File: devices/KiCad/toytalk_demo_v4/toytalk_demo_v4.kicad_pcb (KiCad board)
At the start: 2 copper layers, 55 x 55 mm, 44 parts, among them J1 TYPE-C-31-M-12, J2 Conn_01x02, U1 ESP32-S3-WROOM-1-N8R8, U2 MAX98357AEWL_T, U3 BQ24074RGTR, U4 AP2112K-3.3TRG1, U5 TPS61022RWUR

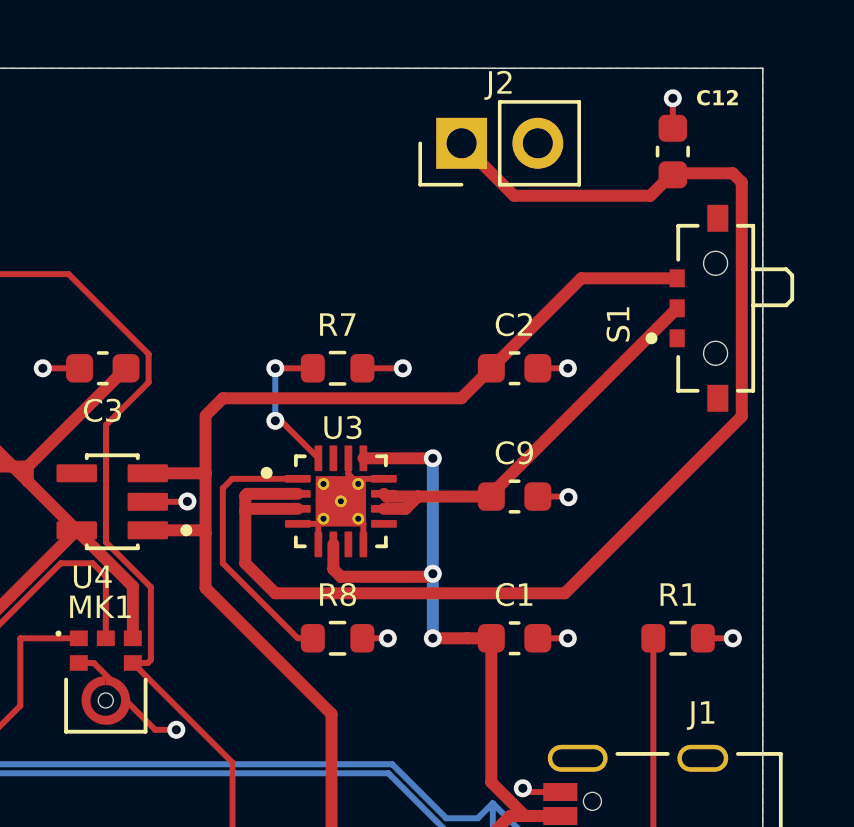
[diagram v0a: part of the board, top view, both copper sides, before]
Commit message: Add toytalk_demo_v4 PCB: fix BQ24074 power issue (EN2→VBUS, ILIM 750Ω)
- Change EN2 from GND to VBUS (AC adapter mode) to remove 500mA input current limit
- Add R10 (750Ω) on ILIM pin for ~1.2A input current limit
- Increase capacitors: C2/C3/C9 to 22uF, C8 to 10uF
- Clean up toytalker_v0.1 firmware comments

Co-Authored-By: Claude Opus 4.6 <noreply@anthropic.com>
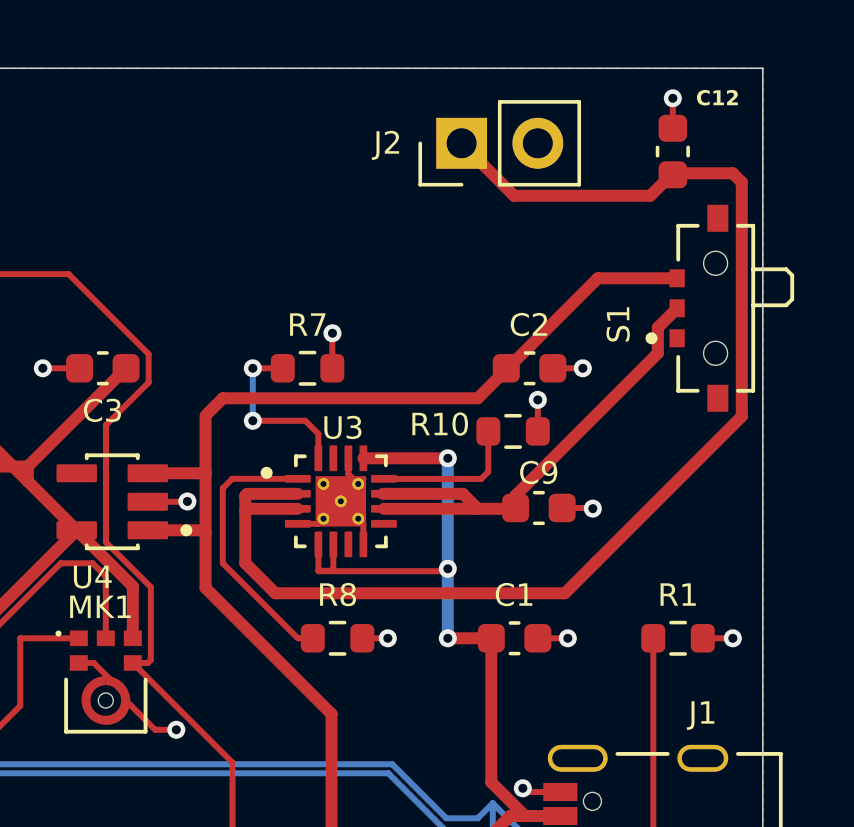
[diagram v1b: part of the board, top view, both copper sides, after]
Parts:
- added R10: 750, Resistor_SMD:R_0603_1608Metric, F.Cu at (58.7, 24.1)
- C2, C3, C9: value 10uF -> 22uF
- C8: value 0.1uF -> 10uF
- R3: value 47R -> 47
- moved R7 1.00 mm to (51.8, 22.0)
- moved C9 0.90 mm to (59.5, 26.7)
- moved C2 0.50 mm to (59.2, 22.0)
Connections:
- U3 pad 12: GND -> Net-(U3-ILIM)
- U3 pad 5: GND -> VBUS
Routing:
- net Net-(U3-ILIM): track 0.00 -> 4.88 mm
- net /V_SYS: track 13.8 -> 16.7 mm
- net VBUS: track 52.8 -> 55.1 mm
- net Net-(U3-ISET): track 4.95 -> 5.93 mm
- net GND: track 79.9 -> 79.6 mm, vias 29 -> 30
